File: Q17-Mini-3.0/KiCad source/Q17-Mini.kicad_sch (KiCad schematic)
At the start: 82 parts, among them J1 INPUT, J2-1 SPK+, J2-2 SPK-, J3-1 V+, J3-2 GND, J3-3 V-, Q1 IRF610, Q10 KSA992, Q12 KSC1845, Q13 IRF610, Q14 IRF9610, Q15 FQA46N15, Q16 IXTQ36P15P, Q2 KSA992, Q3 KSC1845, Q4 IRF9610, Q5 FQPF7P20, Q6 2SK3564, Q7 LSK170B, Q8 DN2540, Q9 BS250P, U1 OPA1611, U2 NDC7003P

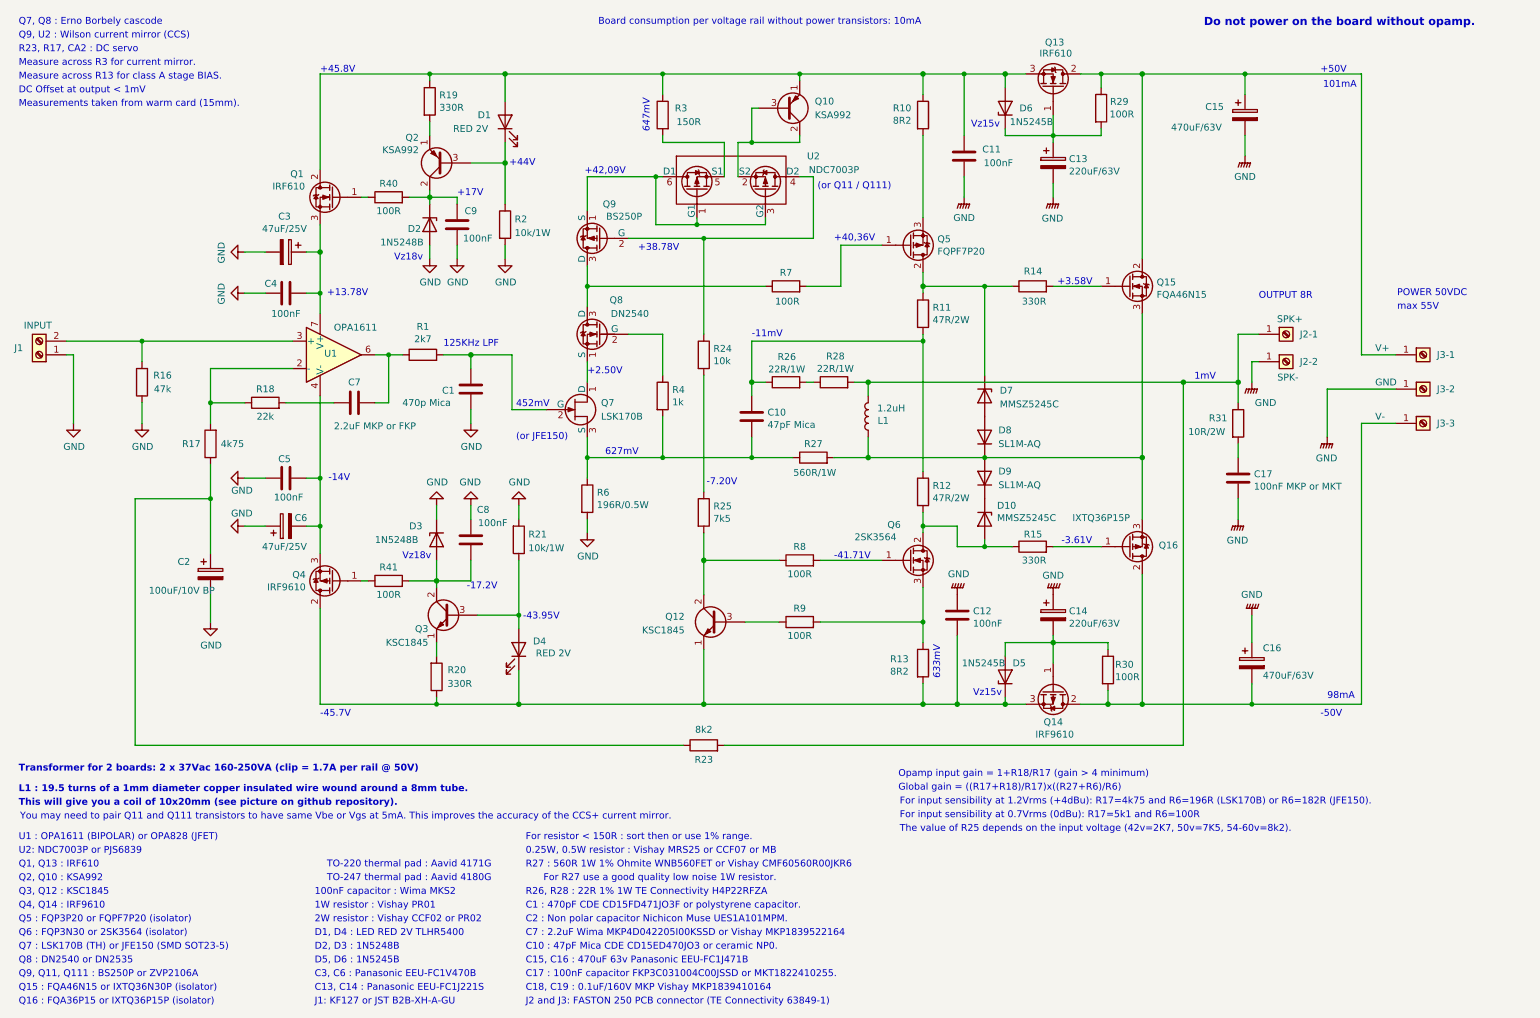
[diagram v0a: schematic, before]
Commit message: Update Q17-Mini to 3.0.3
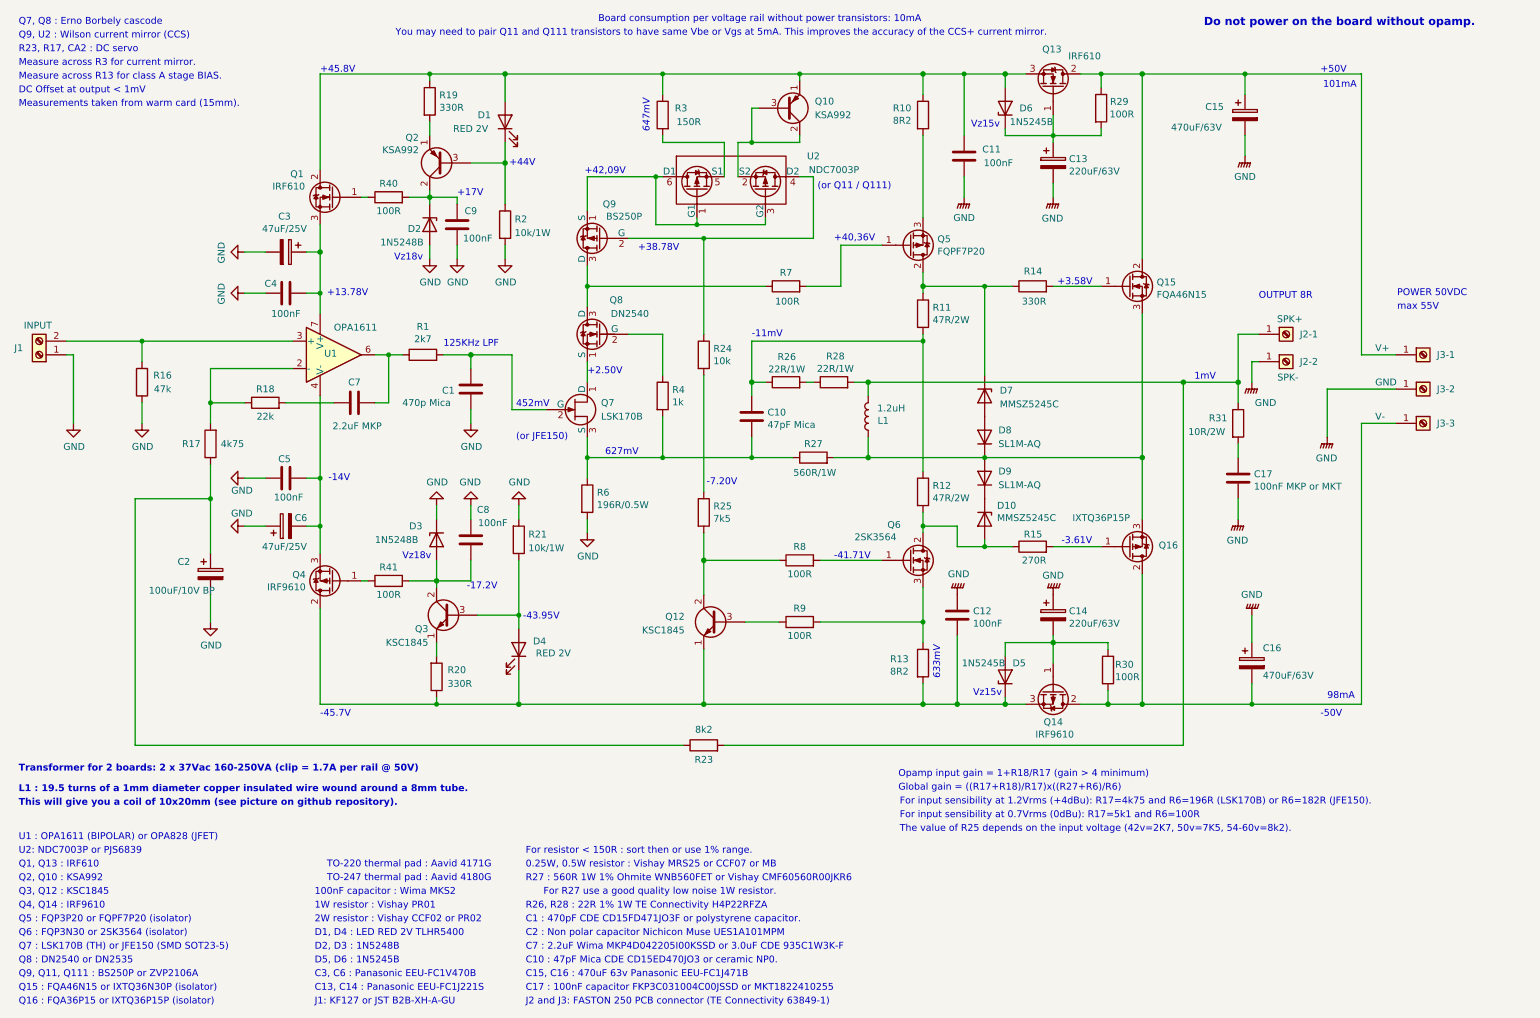
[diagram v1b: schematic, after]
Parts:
- C3, C6: footprint Capacitor_THT:CP_Radial_D10.0mm_P5.00mm -> Capacitor_THT:CP_Radial_D10.0mm_P2.50mm_P5.00mm
- C7: value 2.2uF MKP or FKP -> 2.2uF MKP
- R15: value 330R -> 270R; Mouser 594-MRS25000C3300FCT -> 594-MRS25000C2700FCT; Part# MRS25000C3300FCT00 -> MRS25000C2700FCT00
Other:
- note added: "C17 : 100nF capacitor FKP3C031004C00JSSD or MKT1822410255"
- note added: "C2 : Non polar capacitor Nichicon Muse UES1A101MPM"
- note added: "C7 : 2.2uF Wima MKP4D042205I00KSSD or 3.0uF CDE 935C1W3K-F"
- note removed: "C17 : 100nF capacitor FKP3C031004C00JSSD or MKT1822410255."
- note removed: "C18, C19 : 0.1uF/160V MKP Vishay MKP1839410164"
- note removed: "C2 : Non polar capacitor Nichicon Muse UES1A101MPM."
- note removed: "C7 : 2.2uF Wima MKP4D042205I00KSSD or Vishay MKP1839522164"
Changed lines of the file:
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@@
 	(title_block
 		(title "Q17-Mini Amplifier")
-		(date "2024-08-31")
+		(date "2024-09-14")
 		(rev "2.3.5")
 		(company "Principe circuit by Tiberiu Vicol")
@@
 	(text "R26, R28 : 22R 1% 1W TE Connectivity H4P22RFZA"
 		(exclude_from_sim no)
-		(at 107.95 176.53 0)
+		(at 107.95 179.07 0)
 		(effects
 			(font
@@
 		)
 	)
-	(text "C2 : Non polar capacitor Nichicon Muse UES1A101MPM."
+	(text "C2 : Non polar capacitor Nichicon Muse UES1A101MPM"
 		(exclude_from_sim no)
-		(at 107.95 181.61 0)
+		(at 107.95 184.15 0)
 		(effects
 			(font
@@
 	(text "Board consumption per voltage rail without power transistors: 10mA"
 		(exclude_from_sim no)
-		(at 121.412 15.24 0)
+		(at 121.412 14.732 0)
 		(effects
 			(font
@@
 	(text "For resistor < 150R : sort then or use 1% range."
 		(exclude_from_sim no)
-		(at 107.95 166.37 0)
+		(at 107.95 168.91 0)
 		(effects
 			(font
@@
 	(text "For R27 use a good quality low noise 1W resistor."
 		(exclude_from_sim no)
-		(at 132.842 173.228 0)
+		(at 132.842 175.768 0)
 		(effects
 			(font
@@
 	(text "C15, C16 : 470uF 63v Panasonic EEU-FC1J471B"
 		(exclude_from_sim no)
-		(at 107.95 189.23 0)
+		(at 107.95 191.77 0)
 		(effects
 			(font
@@
 		)
 	)
-	(text "C18, C19 : 0.1uF/160V MKP Vishay MKP1839410164"
+	(text "C17 : 100nF capacitor FKP3C031004C00JSSD or MKT1822410255"
 		(exclude_from_sim no)
 		(at 107.95 194.31 0)
@@
 		)
 	)
-	(text "C17 : 100nF capacitor FKP3C031004C00JSSD or MKT1822410255."
-		(exclude_from_sim no)
-		(at 107.95 191.77 0)
-		(effects
-			(font
-				(size 1.27 1.27)
-			)
-			(justify left bottom)
-		)
-	)
 	(text "0.25W, 0.5W resistor : Vishay MRS25 or CCF07 or MB"
 		(exclude_from_sim no)
-		(at 107.95 168.91 0)
+		(at 107.95 171.45 0)
 		(effects
 			(font
@@
 		)
 	)
-	(text "C7 : 2.2uF Wima MKP4D042205I00KSSD or Vishay MKP1839522164"
+	(text "C7 : 2.2uF Wima MKP4D042205I00KSSD or 3.0uF CDE 935C1W3K-F"
 		(exclude_from_sim no)
-		(at 107.95 184.15 0)
+		(at 107.95 186.69 0)
 		(effects
 			(font
@@
 	(text "C1 : 470pF CDE CD15FD471JO3F or polystyrene capacitor."
 		(exclude_from_sim no)
-		(at 107.95 179.07 0)
+		(at 107.95 181.61 0)
 		(effects
 			(font
@@
 	(text "You may need to pair Q11 and Q111 transistors to have same Vbe or Vgs at 5mA. This improves the accuracy of the CCS+ current mirror.\n"
 		(exclude_from_sim no)
-		(at 14.224 162.56 0)
+		(at 83.82 17.272 0)
 		(effects
 			(font
@@
 	(text "R27 : 560R 1W 1% Ohmite WNB560FET or Vishay CMF60560R00JKR6"
 		(exclude_from_sim no)
-		(at 107.95 171.45 0)
+		(at 107.95 173.99 0)
 		(effects
 			(font
@@
 	(text "C10 : 47pF Mica CDE CD15ED470JO3 or ceramic NP0."
 		(exclude_from_sim no)
-		(at 107.95 186.69 0)
+		(at 107.95 189.23 0)
 		(effects
 			(font
@@
 			)
 		)
-		(property "Value" "330R"
+		(property "Value" "270R"
 			(at 204.47 114.3 90)
 			(effects
@@
 			)
 		)
-		(property "Part#" "MRS25000C3300FCT00"
+		(property "Part#" "MRS25000C2700FCT00"
 			(at 201.93 111.76 90)
 			(effects
@@
 			)
 		)
-		(property "Mouser" "594-MRS25000C3300FCT"
+		(property "Mouser" "594-MRS25000C2700FCT"
 			(at 201.93 111.76 90)
 			(effects
@@
 			)
 		)
-		(property "Footprint" "Capacitor_THT:CP_Radial_D10.0mm_P5.00mm"
+		(property "Footprint" "Capacitor_THT:CP_Radial_D10.0mm_P2.50mm_P5.00mm"
 			(at 67.31 106.9848 0)
 			(effects
@@
 			)
 		)
-		(property "Value" "2.2uF MKP or FKP"
-			(at 80.01 89.408 90)
+		(property "Value" "2.2uF MKP"
+			(at 76.708 89.408 90)
 			(effects
 				(font
@@
 			)
 		)
-		(property "Footprint" "Capacitor_THT:CP_Radial_D10.0mm_P5.00mm"
+		(property "Footprint" "Capacitor_THT:CP_Radial_D10.0mm_P2.50mm_P5.00mm"
 			(at 59.69 58.1152 0)
 			(effects
@@
 		(dnp no)
 		(property "Reference" "Q13"
-			(at 204.216 18.2753 90)
+			(at 203.708 19.558 90)
 			(effects
 				(font
@@
 		)
 		(property "Value" "IRF610"
-			(at 203.2 20.32 90)
+			(at 208.534 20.828 90)
 			(effects
 				(font

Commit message: Update Q17-Mini to 3.0.4
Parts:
- Q6: value 2SK3564 -> FQPF3N80C; Mouser 757-2SK3564STA4QM -> 512-FQPF3N80C; Part# 2SK3564(STA4,Q,M) -> FQPF3N80C
- U1: value OPA1611 -> OPA828; Mouser 595-OPA1611AIDR -> 595-OPA828IDR; Part# OPA1611AIDR -> OPA828IDR
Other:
- note added: "-13.86V"
- note added: "Q5 : FQP3P20 (isolator) or FQPF7P20"
- note added: "Q6 : FQP3N30 (isolator) or FQPF3N80C"
- note removed: "-14V"
- note removed: "Q5 : FQP3P20 or FQPF7P20 (isolator)"
- note removed: "Q6 : FQP3N30 or 2SK3564 (isolator)"
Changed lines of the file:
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@@
 	(title_block
 		(title "Q17-Mini Amplifier")
-		(date "2024-09-14")
-		(rev "2.3.5")
+		(date "2024-10-07")
+		(rev "2.3.7")
 		(company "Principe circuit by Tiberiu Vicol")
 		(comment 1 "Modified by Stef for the Q17-Mini project")
@@
 		)
 	)
-	(text "Q5 : FQP3P20 or FQPF7P20 (isolator)"
+	(text "Q5 : FQP3P20 (isolator) or FQPF7P20"
 		(exclude_from_sim no)
 		(at 13.97 181.61 0)
@@
 		)
 	)
-	(text "Q6 : FQP3N30 or 2SK3564 (isolator)"
+	(text "Q6 : FQP3N30 (isolator) or FQPF3N80C"
 		(exclude_from_sim no)
 		(at 13.97 184.15 0)
@@
 		)
 	)
-	(text "-14V"
+	(text "-13.86V"
 		(exclude_from_sim no)
 		(at 71.374 99.822 0)
@@
 		(dnp no)
 		(property "Reference" "U2"
-			(at 161.29 39.37 0)
+			(at 160.782 38.862 0)
 			(effects
 				(font
@@
 		)
 		(property "Value" "NDC7003P"
-			(at 165.1 41.91 0)
+			(at 164.592 41.402 0)
 			(effects
 				(font
@@
 			)
 		)
-		(property "Value" "2SK3564"
-			(at 168.91 109.982 0)
+		(property "Value" "FQPF3N80C"
+			(at 166.624 109.982 0)
 			(effects
 				(font
@@
 			)
 		)
-		(property "Part#" "2SK3564(STA4,Q,M)"
+		(property "Part#" "FQPF3N80C"
 			(at 179.07 114.3 0)
 			(effects
@@
 			)
 		)
-		(property "Mouser" "757-2SK3564STA4QM"
+		(property "Mouser" "512-FQPF3N80C"
 			(at 179.07 114.3 0)
 			(effects
@@
 			)
 		)
-		(property "Value" "OPA1611"
+		(property "Value" "OPA828"
 			(at 72.39 71.12 0)
 			(effects
@@
 			)
 		)
-		(property "Datasheet" "https://www.ti.com/general/docs/suppproductinfo.tsp?distId=26&gotoUrl=https://www.ti.com/lit/gpn/opa1611"
+		(property "Datasheet" "https://www.ti.com/lit/gpn/opa828"
 			(at 72.39 76.2 0)
 			(effects
@@
 			)
 		)
-		(property "Part#" "OPA1611AIDR"
+		(property "Part#" "OPA828IDR"
 			(at 72.39 76.2 0)
 			(effects
@@
 			)
 		)
-		(property "Mouser" "595-OPA1611AIDR"
+		(property "Mouser" "595-OPA828IDR"
 			(at 72.39 76.2 0)
 			(effects
